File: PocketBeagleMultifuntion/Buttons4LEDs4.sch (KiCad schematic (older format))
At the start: 22 parts, among them U11 TC4426, U12 TC4426, U13 74HCT14

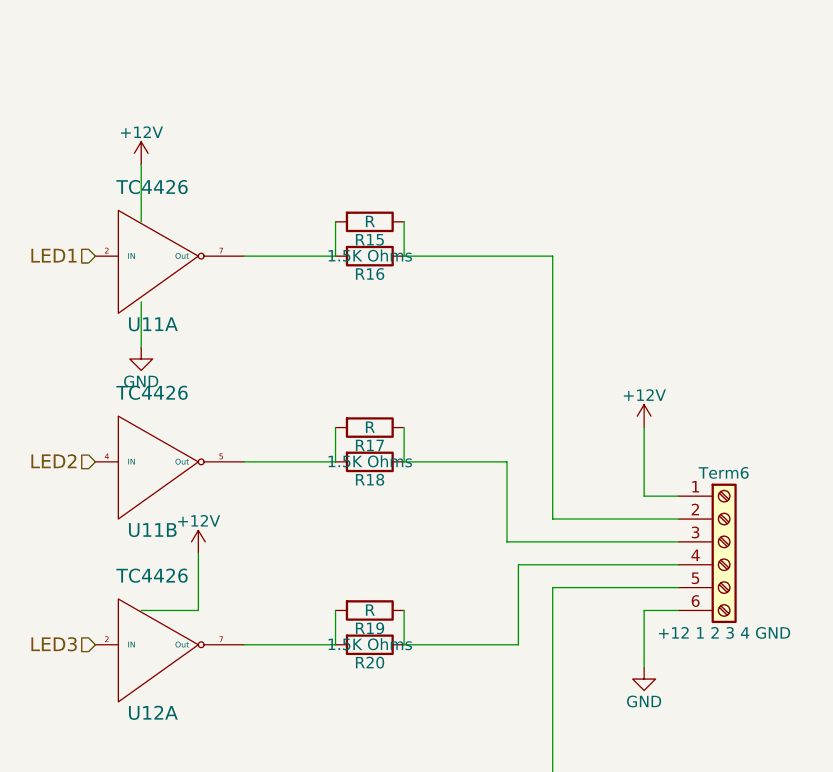
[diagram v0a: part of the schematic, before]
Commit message: Isolate buffer outputs from +12 supply. on the Pocket Beagle Multifunction Board.
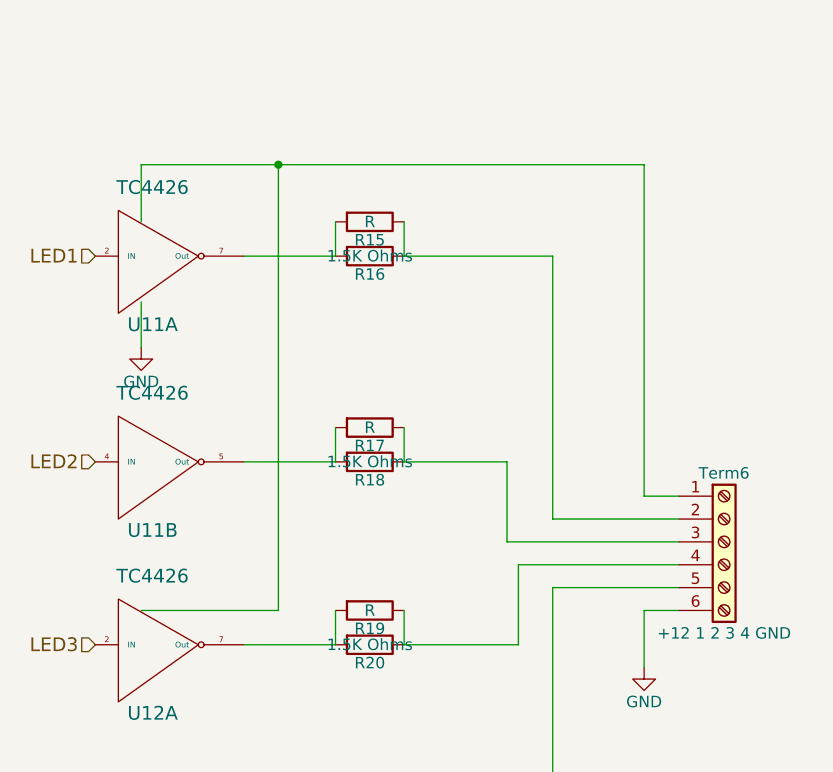
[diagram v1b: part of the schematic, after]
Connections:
- net +12V renamed Vdd
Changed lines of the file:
@@
 $EndComp
 $Comp
-L +12V #PWR055
-U 1 1 60CEB7C8
-P 2550 1650
-F 0 "#PWR055" H 2550 1500 50  0001 C CNN
-F 1 "+12V" H 2550 1790 50  0000 C CNN
-F 2 "" H 2550 1650 50  0001 C CNN
-F 3 "" H 2550 1650 50  0001 C CNN
-	1    2550 1650
-	1    0    0    -1
-$EndComp
-$Comp
-L +12V #PWR056
-U 1 1 60CEB860
-P 2800 3350
-F 0 "#PWR056" H 2800 3200 50  0001 C CNN
-F 1 "+12V" H 2800 3490 50  0000 C CNN
-F 2 "" H 2800 3350 50  0001 C CNN
-F 3 "" H 2800 3350 50  0001 C CNN
-	1    2800 3350
-	1    0    0    -1
-$EndComp
-$Comp
-L GND #PWR057
+L GND #PWR055
 U 1 1 60CEB8BC
 P 2550 2450
-F 0 "#PWR057" H 2550 2200 50  0001 C CNN
+F 0 "#PWR055" H 2550 2200 50  0001 C CNN
 F 1 "GND" H 2550 2300 50  0000 C CNN
 F 2 "" H 2550 2450 50  0001 C CNN
@@
 $EndComp
 $Comp
-L GND #PWR058
+L GND #PWR056
 U 1 1 60CEB954
 P 2550 5150
-F 0 "#PWR058" H 2550 4900 50  0001 C CNN
+F 0 "#PWR056" H 2550 4900 50  0001 C CNN
 F 1 "GND" H 2550 5000 50  0000 C CNN
 F 2 "" H 2550 5150 50  0001 C CNN
@@
 $EndComp
 $Comp
-L +12V #PWR059
-U 1 1 60CEBB98
-P 4750 2800
-F 0 "#PWR059" H 4750 2650 50  0001 C CNN
-F 1 "+12V" H 4750 2940 50  0000 C CNN
-F 2 "" H 4750 2800 50  0001 C CNN
-F 3 "" H 4750 2800 50  0001 C CNN
-	1    4750 2800
-	1    0    0    -1
-$EndComp
-$Comp
-L GND #PWR060
+L GND #PWR057
 U 1 1 60CEBBCA
 P 4750 3850
-F 0 "#PWR060" H 4750 3600 50  0001 C CNN
+F 0 "#PWR057" H 4750 3600 50  0001 C CNN
 F 1 "GND" H 4750 3700 50  0000 C CNN
 F 2 "" H 4750 3850 50  0001 C CNN
@@
 $EndComp
 $Comp
-L GND #PWR061
+L GND #PWR058
 U 1 1 60CEC8C9
 P 4000 6250
-F 0 "#PWR061" H 4000 6000 50  0001 C CNN
+F 0 "#PWR058" H 4000 6000 50  0001 C CNN
 F 1 "GND" H 4000 6100 50  0000 C CNN
 F 2 "" H 4000 6250 50  0001 C CNN
@@
 NoConn ~ 4900 5950
 $Comp
-L +3V3 #PWR062
+L +3V3 #PWR059
 U 1 1 60CECA8D
 P 4400 5350
-F 0 "#PWR062" H 4400 5200 50  0001 C CNN
+F 0 "#PWR059" H 4400 5200 50  0001 C CNN
 F 1 "+3V3" H 4400 5490 50  0000 C CNN
 F 2 "" H 4400 5350 50  0001 C CNN
@@
 $EndComp
 $Comp
-L GND #PWR063
+L GND #PWR060
 U 1 1 60CEE082
 P 6450 3800
-F 0 "#PWR063" H 6450 3550 50  0001 C CNN
+F 0 "#PWR060" H 6450 3550 50  0001 C CNN
 F 1 "GND" H 6450 3650 50  0000 C CNN
 F 2 "" H 6450 3800 50  0001 C CNN
@@
 $EndComp
 $Comp
-L +3V3 #PWR064
+L +3V3 #PWR061
 U 1 1 60CF063B
 P 6700 1200
-F 0 "#PWR064" H 6700 1050 50  0001 C CNN
+F 0 "#PWR061" H 6700 1050 50  0001 C CNN
 F 1 "+3V3" H 6700 1340 50  0000 C CNN
 F 2 "" H 6700 1200 50  0001 C CNN
@@
 $EndComp
 $Comp
-L +3V3 #PWR065
+L +3V3 #PWR062
 U 1 1 60CF0689
 P 6950 2250
-F 0 "#PWR065" H 6950 2100 50  0001 C CNN
+F 0 "#PWR062" H 6950 2100 50  0001 C CNN
 F 1 "+3V3" H 6950 2390 50  0000 C CNN
 F 2 "" H 6950 2250 50  0001 C CNN
@@
 $EndComp
 $Comp
-L +3V3 #PWR066
+L +3V3 #PWR063
 U 1 1 60CF0833
 P 6850 3100
-F 0 "#PWR066" H 6850 2950 50  0001 C CNN
+F 0 "#PWR063" H 6850 2950 50  0001 C CNN
 F 1 "+3V3" H 6850 3240 50  0000 C CNN
 F 2 "" H 6850 3100 50  0001 C CNN
@@
 $EndComp
 $Comp
-L +3V3 #PWR067
+L +3V3 #PWR064
 U 1 1 60CF0A78
 P 6750 4050
-F 0 "#PWR067" H 6750 3900 50  0001 C CNN
+F 0 "#PWR064" H 6750 3900 50  0001 C CNN
 F 1 "+3V3" H 6750 4190 50  0000 C CNN
 F 2 "" H 6750 4050 50  0001 C CNN
@@
 $EndComp
 $Comp
-L GND #PWR068
+L GND #PWR065
 U 1 1 60CF0DB8
 P 6550 2250
-F 0 "#PWR068" H 6550 2000 50  0001 C CNN
+F 0 "#PWR065" H 6550 2000 50  0001 C CNN
 F 1 "GND" H 6550 2100 50  0000 C CNN
 F 2 "" H 6550 2250 50  0001 C CNN
@@
 $EndComp
 $Comp
-L GND #PWR069
+L GND #PWR066
 U 1 1 60CF0EEE
 P 6700 3050
-F 0 "#PWR069" H 6700 2800 50  0001 C CNN
+F 0 "#PWR066" H 6700 2800 50  0001 C CNN
 F 1 "GND" H 6700 2900 50  0000 C CNN
 F 2 "" H 6700 3050 50  0001 C CNN
@@
 $EndComp
 $Comp
-L GND #PWR070
+L GND #PWR067
 U 1 1 60CF1041
 P 6850 4000
-F 0 "#PWR070" H 6850 3750 50  0001 C CNN
+F 0 "#PWR067" H 6850 3750 50  0001 C CNN
 F 1 "GND" H 6850 3850 50  0000 C CNN
 F 2 "" H 6850 4000 50  0001 C CNN
@@
 $EndComp
 $Comp
-L GND #PWR071
+L GND #PWR068
 U 1 1 60CF113D
 P 6750 5050
-F 0 "#PWR071" H 6750 4800 50  0001 C CNN
+F 0 "#PWR068" H 6750 4800 50  0001 C CNN
 F 1 "GND" H 6750 4900 50  0000 C CNN
 F 2 "" H 6750 5050 50  0001 C CNN
@@
 	2550 4850 2550 5150
 Wire Wire Line
-	2550 3600 2800 3600
-Wire Wire Line
-	2800 3600 2800 3350
+	2550 3600 3150 3600
 Wire Wire Line
 	2550 2250 2550 2450
@@
 	2550 1650 2550 1900
 Wire Wire Line
-	4750 2800 4750 3100
+	4750 1650 4750 3100
 Wire Wire Line
 	4750 3100 4900 3100
@@
 Text HLabel 7750 4600 2    60   Output ~ 0
 Button4
+Wire Wire Line
+	2550 1650 4750 1650
+Wire Wire Line
+	3150 3600 3150 1650
+Connection ~ 3150 1650
 $EndSCHEMATC
